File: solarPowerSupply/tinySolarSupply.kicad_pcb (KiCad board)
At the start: 2 copper layers, 39.5 x 22 mm, 16 parts, among them J1 Conn_01x02_Pin, J2 Conn_01x02_Pin, J3 Conn_01x02_Pin, J4 Conn_01x02_Pin, Q1 2N7002, U1 AP3015AKTR-G1

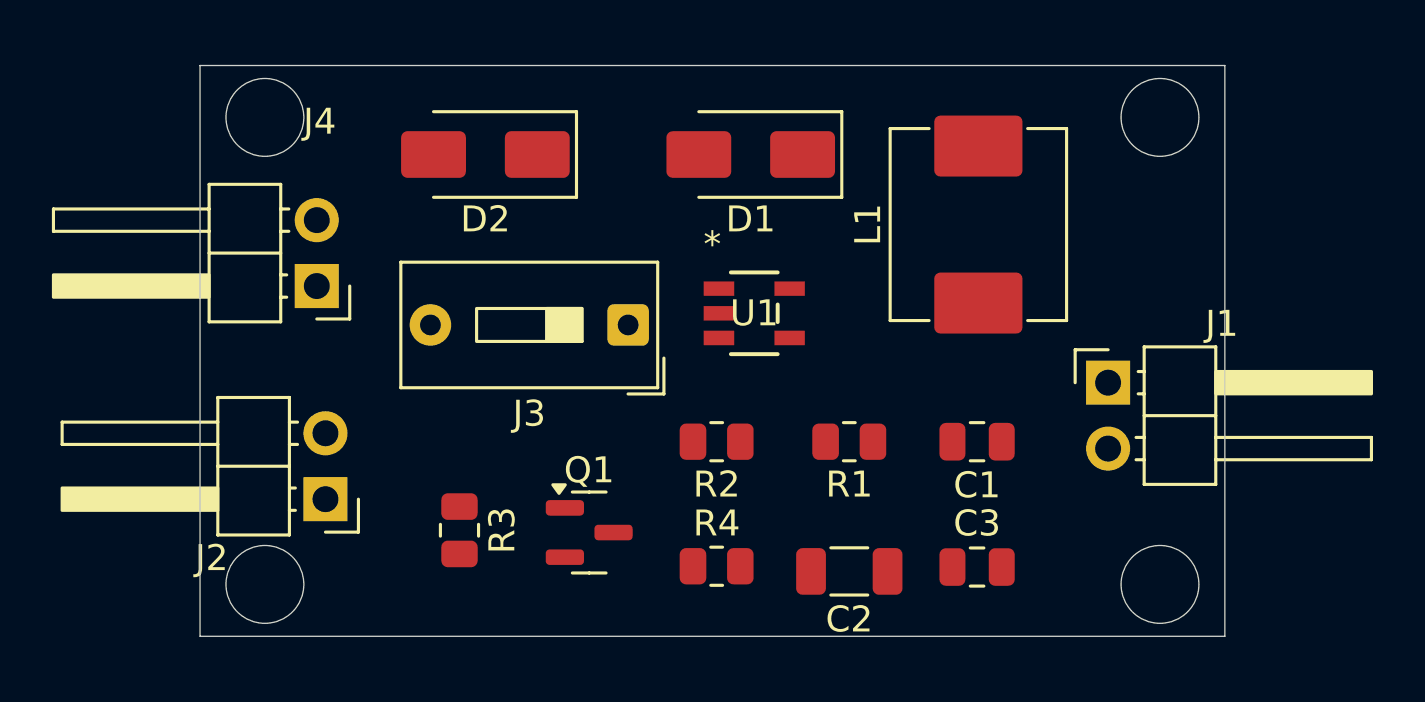
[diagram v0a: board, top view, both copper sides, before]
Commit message: Tiny solar power supply complete schematics and gerber files
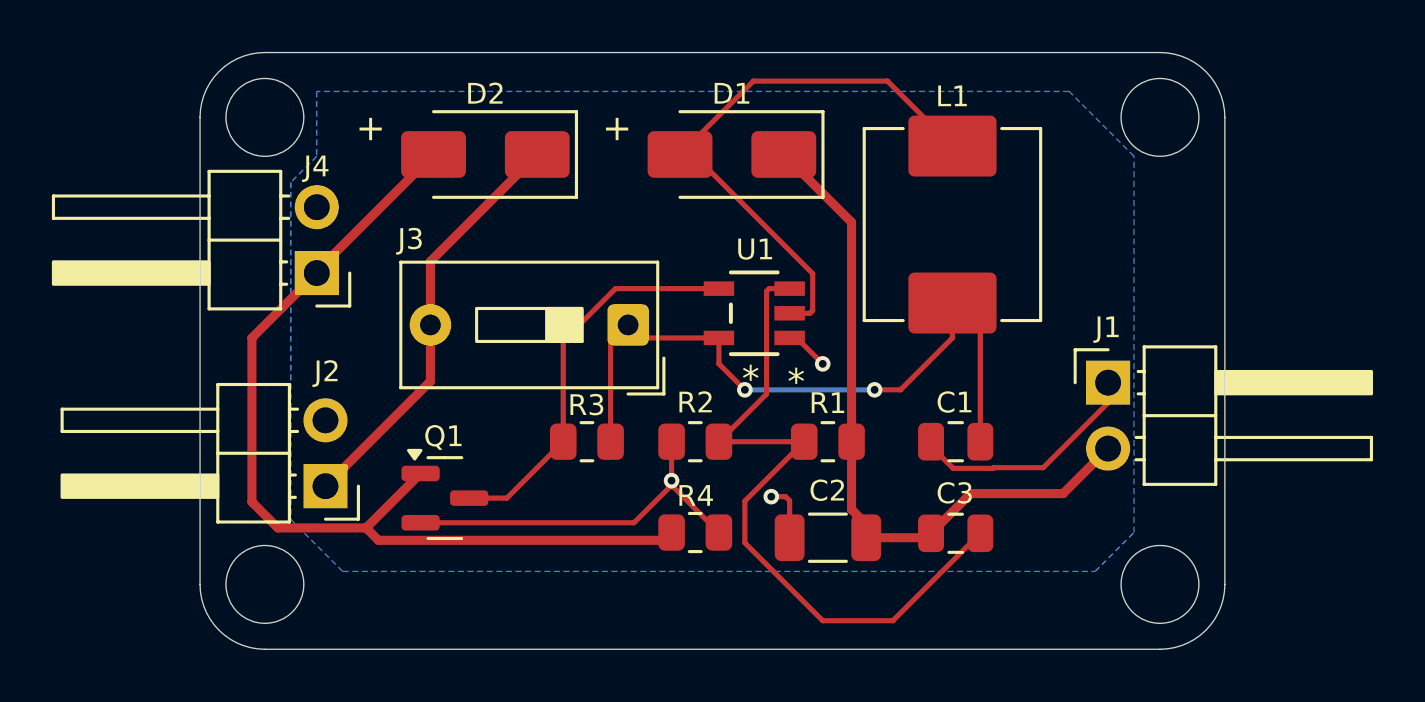
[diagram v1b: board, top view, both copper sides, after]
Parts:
- added REF**: KiCad-Logo2_5mm_SilkScreen, Symbol:KiCad-Logo2_5mm_SilkScreen, B.Cu at (113.0, 152.2)
- moved R3 5.98 mm to (115.4, 148.5), turned to 180 degrees
- moved Q1 5.72 mm to (109.9, 150.7)
- moved C2 1.54 mm to (124.7, 152.2)
- moved C3 1.54 mm to (129.6, 152.0)
- moved R4 1.54 mm to (119.6, 152.0)
- moved L1 1.00 mm to (129.5, 140.1)
- moved R1 0.83 mm to (124.7, 148.5)
- moved C1 0.82 mm to (129.6, 148.5)
- moved R2 0.82 mm to (119.6, 148.5)
- moved D1 0.72 mm to (121.0, 137.4)
- moved J2 0.50 mm to (105.3, 150.2)
- moved J4 0.50 mm to (105.0, 142.0)
- turned U1 to 180 degrees
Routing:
- net /SOLAR_P: track 0.00 -> 36.2 mm
- net GNDD: track 0.00 -> 27.6 mm, vias 0 -> 3
- net Net-(U1-FB): track 0.00 -> 27.3 mm
- net Net-(J3-Pin_1): track 0.00 -> 26.9 mm, vias 0 -> 2
- net /OUT_P: track 0.00 -> 26.8 mm
- net Net-(D1-A): track 0.00 -> 22.1 mm
- net /BAT_P: track 0.00 -> 16.2 mm
- net Net-(Q1-D): track 0.00 -> 15.2 mm
- added copper zone on B.Cu, net GNDD
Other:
- board size 39.5 x 22 mm -> 39.5 x 23 mm
- board text added: "+"
